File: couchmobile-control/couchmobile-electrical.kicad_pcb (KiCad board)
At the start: 2 copper layers, 100 x 100 mm, 50 parts, among them J1 Power_In, J10 Motor1, J11 Motor2, J2 GPIO_NANO_1, J5 ESTOP_IRQ_EN, J6 BNO_COMM_CTRL, J7 Joystick, J8 Encoder1, J9 Encoder2, Q1 PMOS DGS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

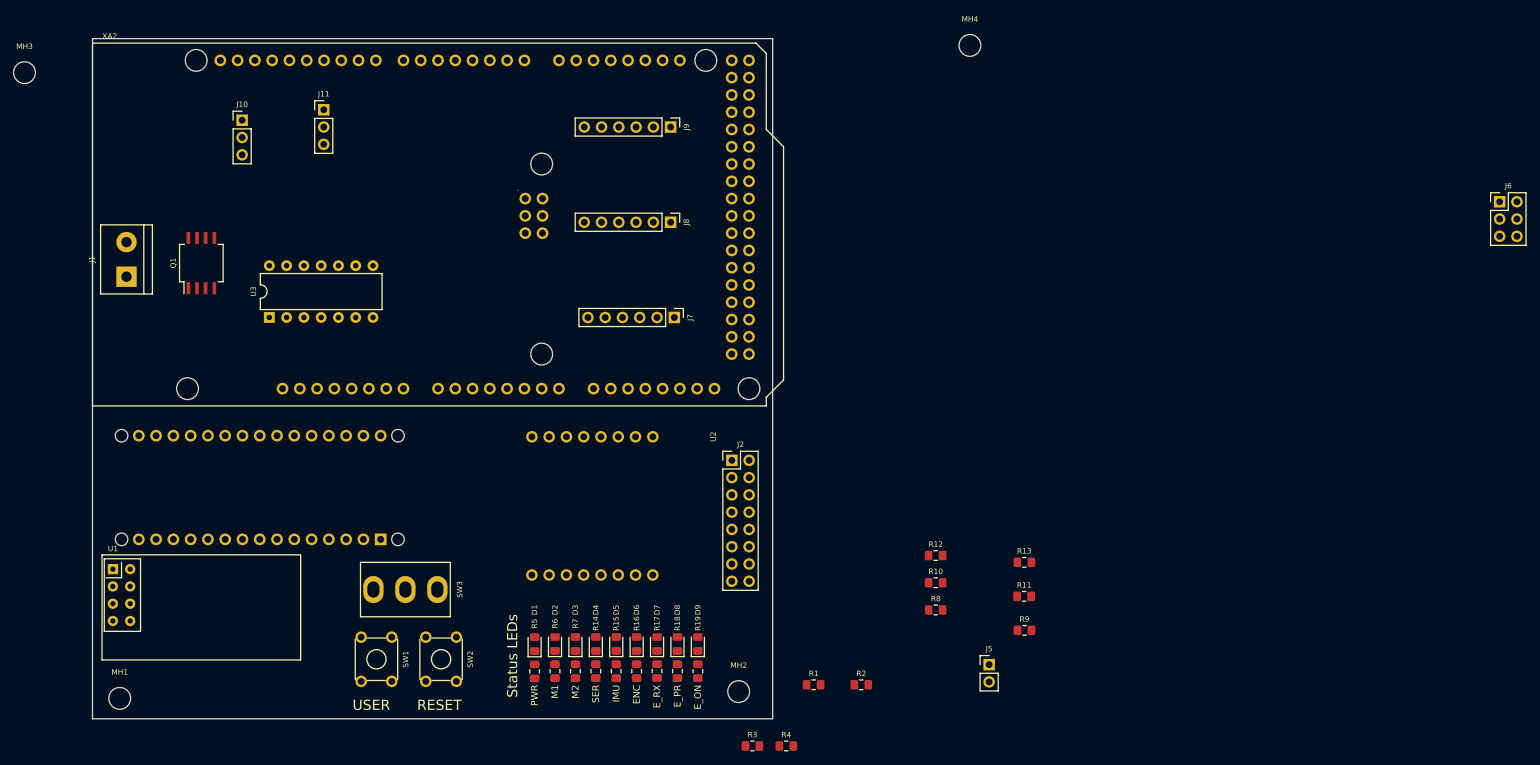
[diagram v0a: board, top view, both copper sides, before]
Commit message: Made and added so8 package for pfet
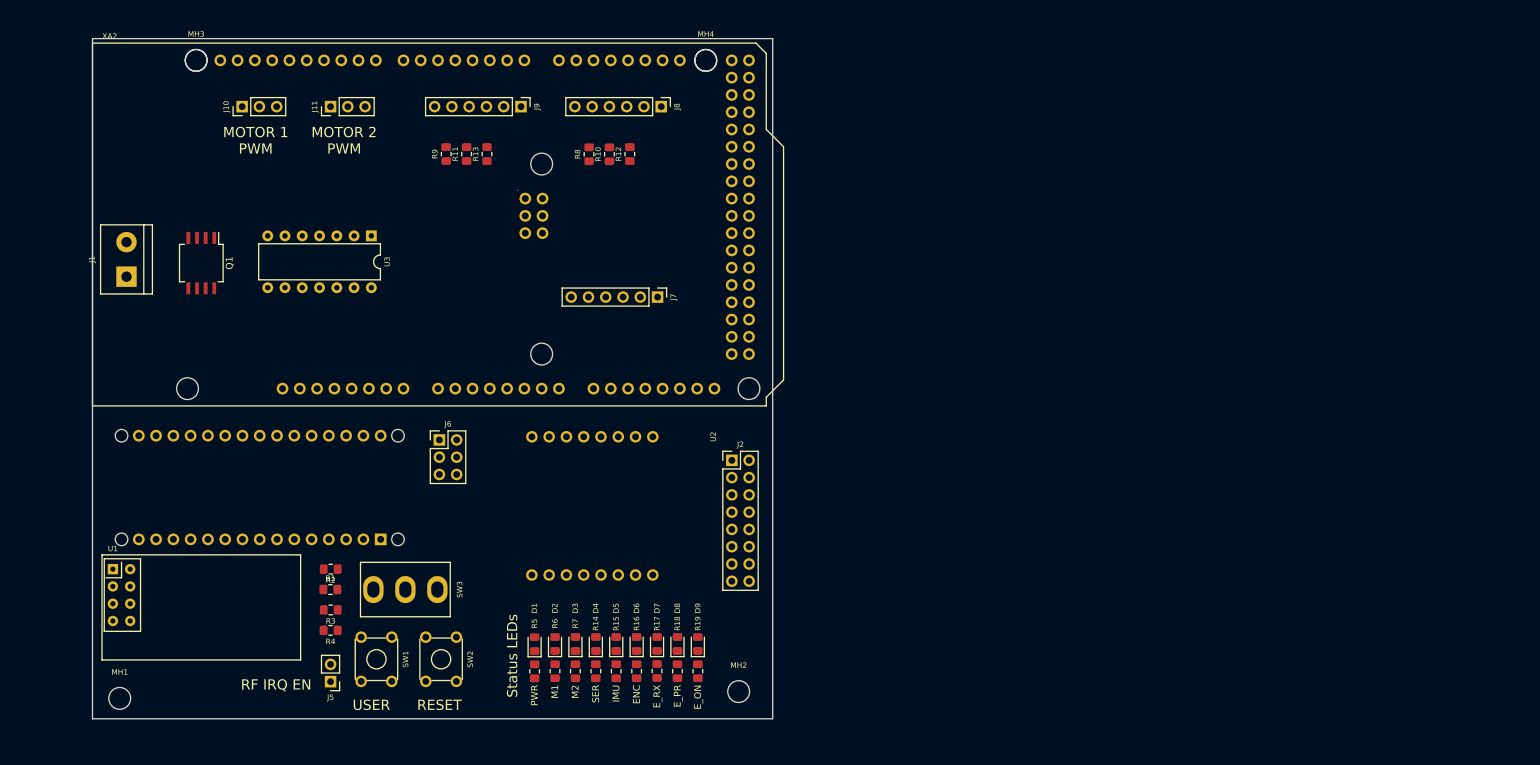
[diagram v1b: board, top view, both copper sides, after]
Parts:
- Q1: footprint Package_SO:SO-8_5.3x6.2mm_P1.27mm -> couch-packages:SO-8_DGS
- moved J6 159.8 mm to (71.0, 79.0)
- moved R9 110.1 mm to (72.0, 37.0), turned to 90 degrees
- moved R11 104.6 mm to (75.0, 37.0), turned to 90 degrees
- moved R13 99.2 mm to (78.0, 37.0), turned to 90 degrees
- moved J5 96.9 mm to (55.0, 114.5), turned to 180 degrees
- moved R8 84.2 mm to (93.0, 37.0), turned to 90 degrees
- moved R2 79.8 mm to (55.0, 98.0), turned to 180 degrees
- moved R10 79.2 mm to (96.0, 37.0), turned to 90 degrees
- moved R12 74.2 mm to (99.0, 37.0), turned to 90 degrees
- moved R1 72.4 mm to (55.0, 101.0)
- moved R4 69.1 mm to (55.0, 107.0), turned to 180 degrees
- moved R3 65.1 mm to (55.0, 104.0), turned to 180 degrees
- moved MH4 38.9 mm to (110.2, 23.2)
- moved MH3 25.3 mm to (35.2, 23.2)
- moved J9 22.2 mm to (83.0, 30.0)
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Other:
- board text added: "MOTOR 1 PWM"
- board text added: "MOTOR 2 PWM"
- board text added: "RF IRQ EN"

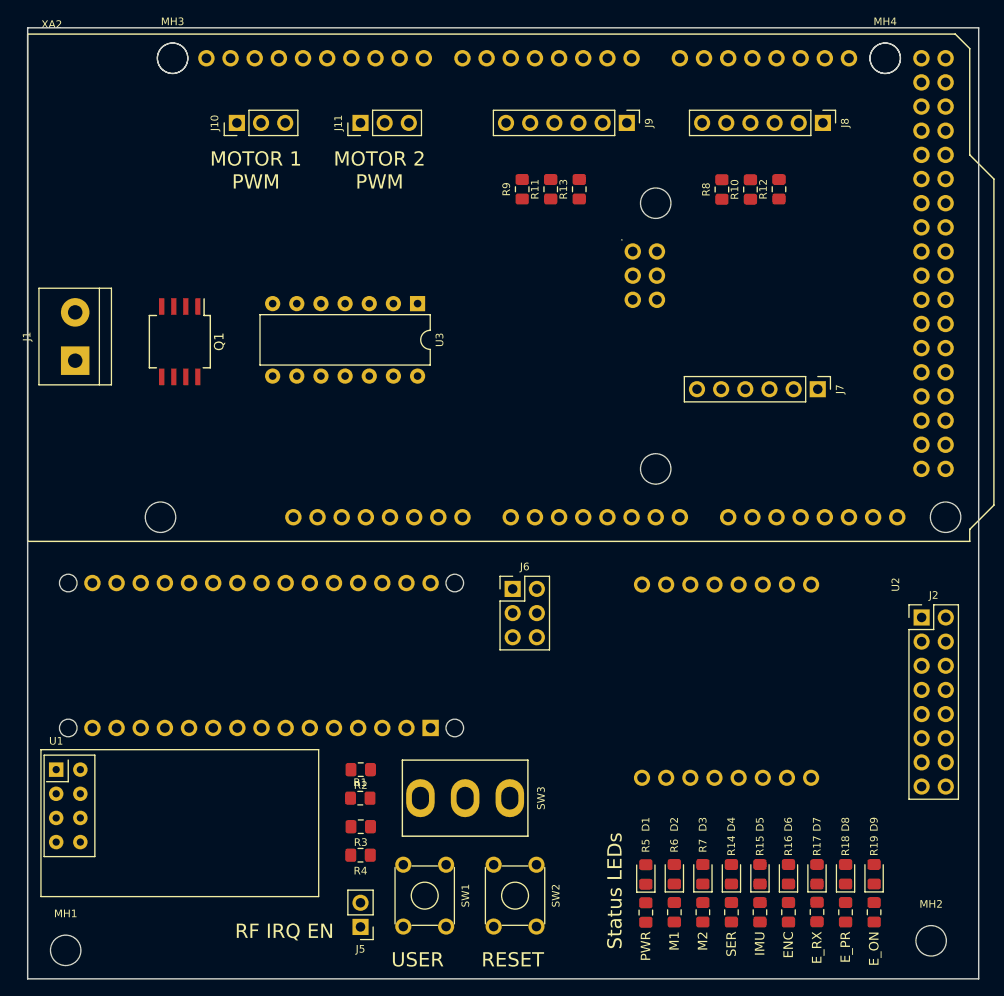
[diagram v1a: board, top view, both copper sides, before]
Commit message: Changed solder to mask clearance to 0.05mm. Wired up half the gpio for nano
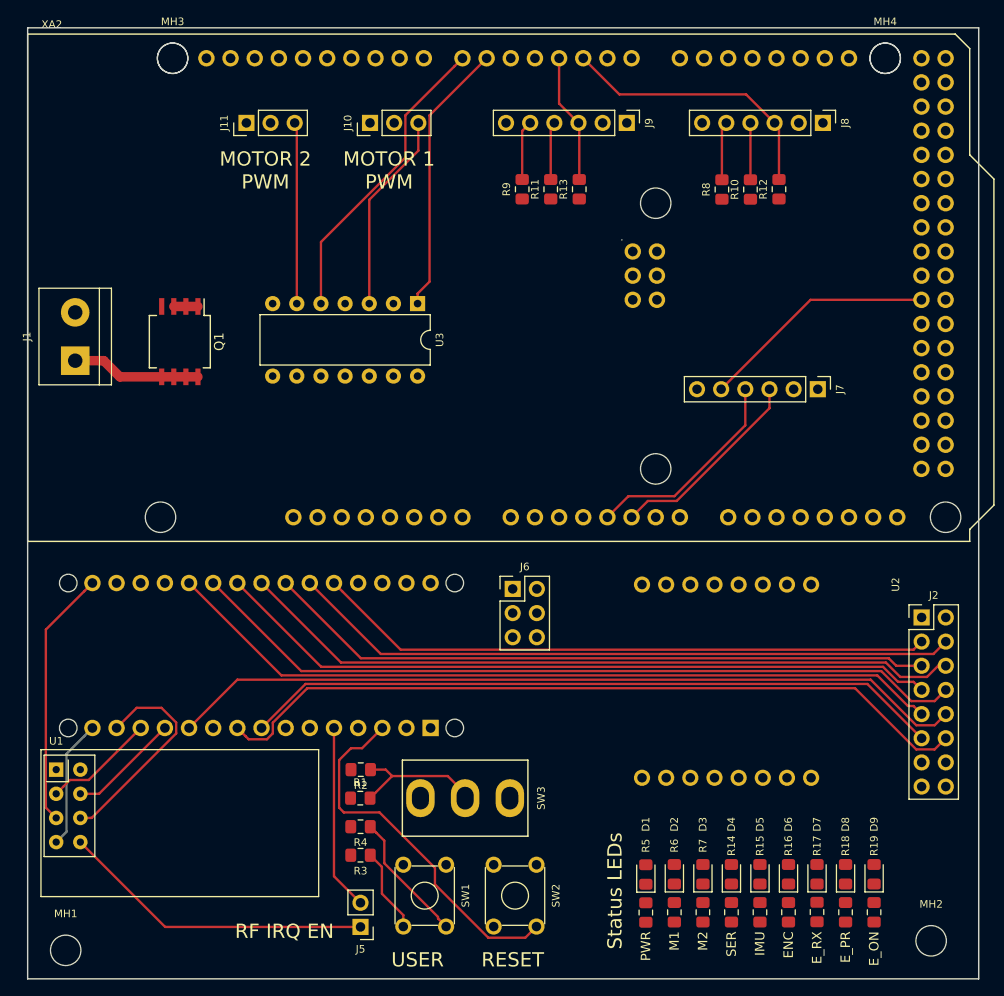
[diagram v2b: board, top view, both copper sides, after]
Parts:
- moved J10 14.0 mm to (56.0, 30.0)
- moved J11 12.0 mm to (43.0, 30.0)
- moved R3 3.00 mm to (55.0, 107.0)
- moved R4 3.00 mm to (55.0, 104.0)
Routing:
- net /NANO_D8: track 0.00 -> 84.1 mm
- net /NANO_A1: track 0.00 -> 82.7 mm
- net /NANO_A2: track 0.00 -> 82.7 mm
- net /ESTOP_HS: track 0.00 -> 81.0 mm
- net /NANO_A3: track 0.00 -> 76.6 mm
- net /NANO_A4: track 0.00 -> 76.5 mm
- net /ESTOP_ON: track 0.00 -> 73.7 mm
- net /NANO_A6: track 0.00 -> 70.5 mm
- net /NANO_A5: track 0.00 -> 70.5 mm
- net /NANO_A7: track 0.00 -> 65.0 mm
- net /NANO_RESET: track 0.00 -> 38.9 mm
- net /ESTOP_IRQ: track 0.00 -> 33.2 mm
- net /PWM_M2: track 0.00 -> 32.0 mm
- net /EN1_1: track 0.00 -> 29.1 mm
- net /PWM_M1: track 0.00 -> 28.8 mm
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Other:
- rule pad_to_mask_clearance: 0.2 -> 0.05

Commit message: Wired up a lot of the busses.
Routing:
- net /STATUS_IMU: track 0.00 -> 114.7 mm, vias 0 -> 2
- net /STATUS_SERIAL: track 0.00 -> 111.8 mm, vias 0 -> 2
- net /STATUS_ENC: track 0.00 -> 110.8 mm, vias 0 -> 2
- net /STATUS_M1: track 0.00 -> 110.7 mm, vias 0 -> 3
- net /STATUS_M2: track 0.00 -> 107.0 mm, vias 0 -> 3
- net /ESTOP_EN: track 0.00 -> 85.6 mm, vias 0 -> 2
- net /ESTOP_RX: track 0.00 -> 80.8 mm, vias 0 -> 2
- net /SCL: track 0.00 -> 68.0 mm, vias 0 -> 1
- net /SDA: track 0.00 -> 65.5 mm, vias 0 -> 1
- net /NANO_TX: track 0.00 -> 60.2 mm
- net /NANO_RX: track 0.00 -> 58.9 mm
- net /NANO_SW1: track 13.8 -> 71.3 mm
- net /ESTOP_TRAN: track 0.00 -> 56.4 mm
- net /IMU_WAKE: track 0.00 -> 53.3 mm, vias 0 -> 1
- net /MEGA_RESET: track 0.00 -> 52.1 mm
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
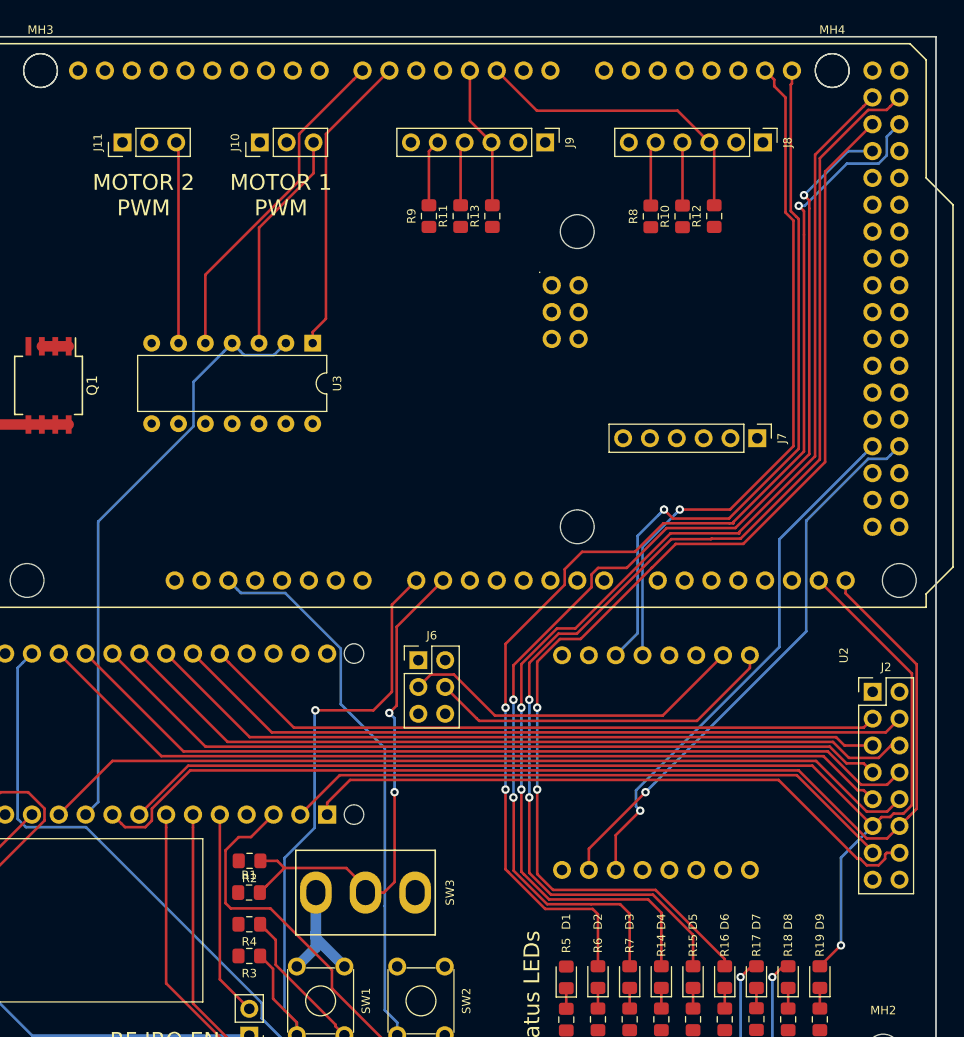
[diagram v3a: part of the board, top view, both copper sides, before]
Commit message: Added 5v to 3.3v line converters.
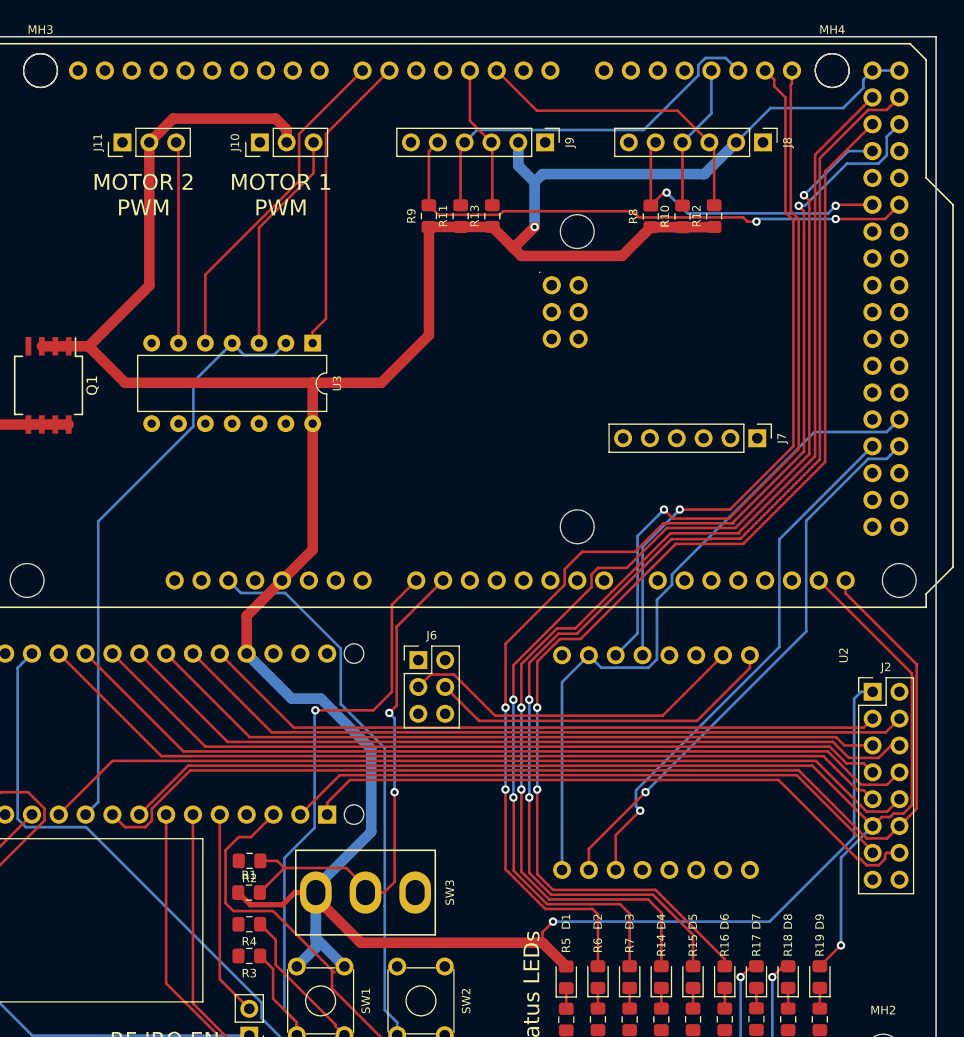
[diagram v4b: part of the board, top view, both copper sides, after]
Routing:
- net +5V: track 14.7 -> 323.7 mm, vias 0 -> 2
- net /IMU_RESET: track 0.00 -> 64.8 mm
- net /EN2_3: track 6.30 -> 52.4 mm, vias 0 -> 2
- net /EN2_2: track 6.11 -> 36.4 mm
- net /EN1_3: track 6.17 -> 28.8 mm, vias 0 -> 2
- net /EN1_2: track 5.98 -> 13.9 mm

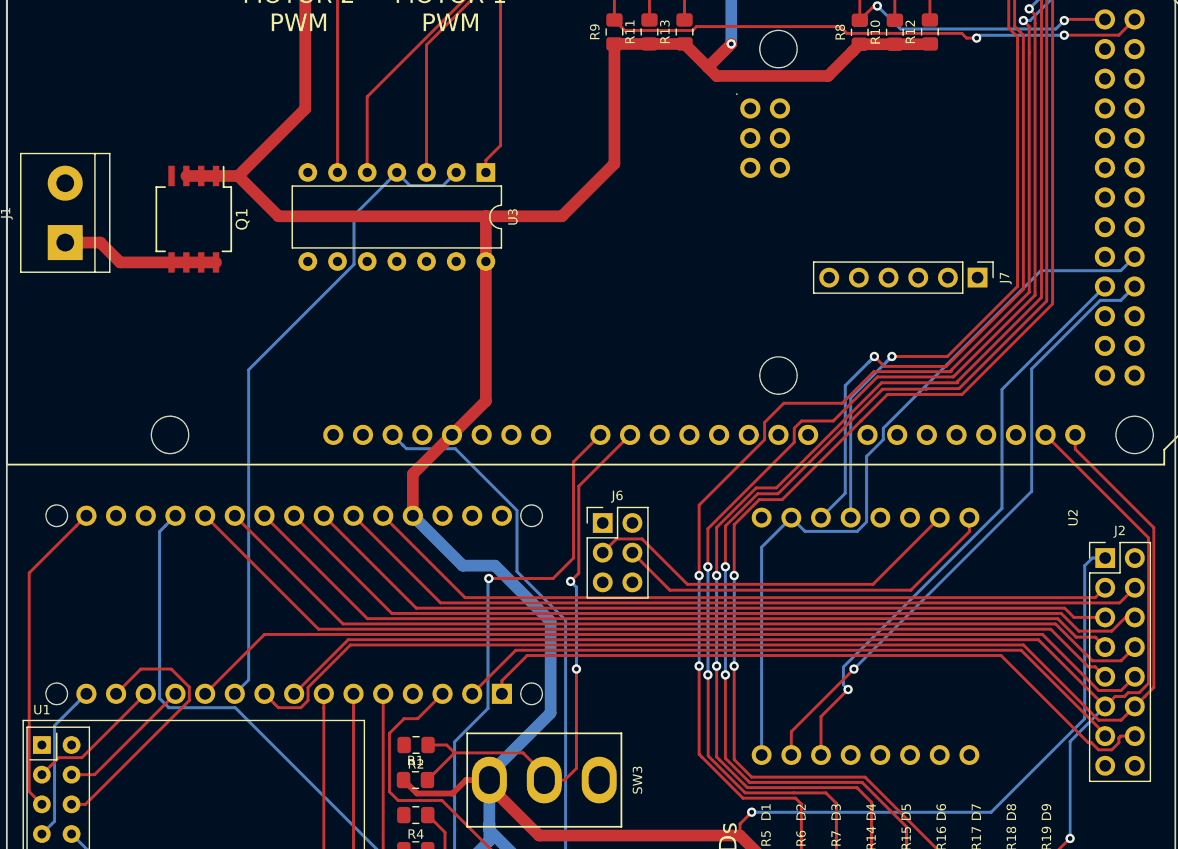
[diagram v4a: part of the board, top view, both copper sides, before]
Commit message: Laid out most lines except ground
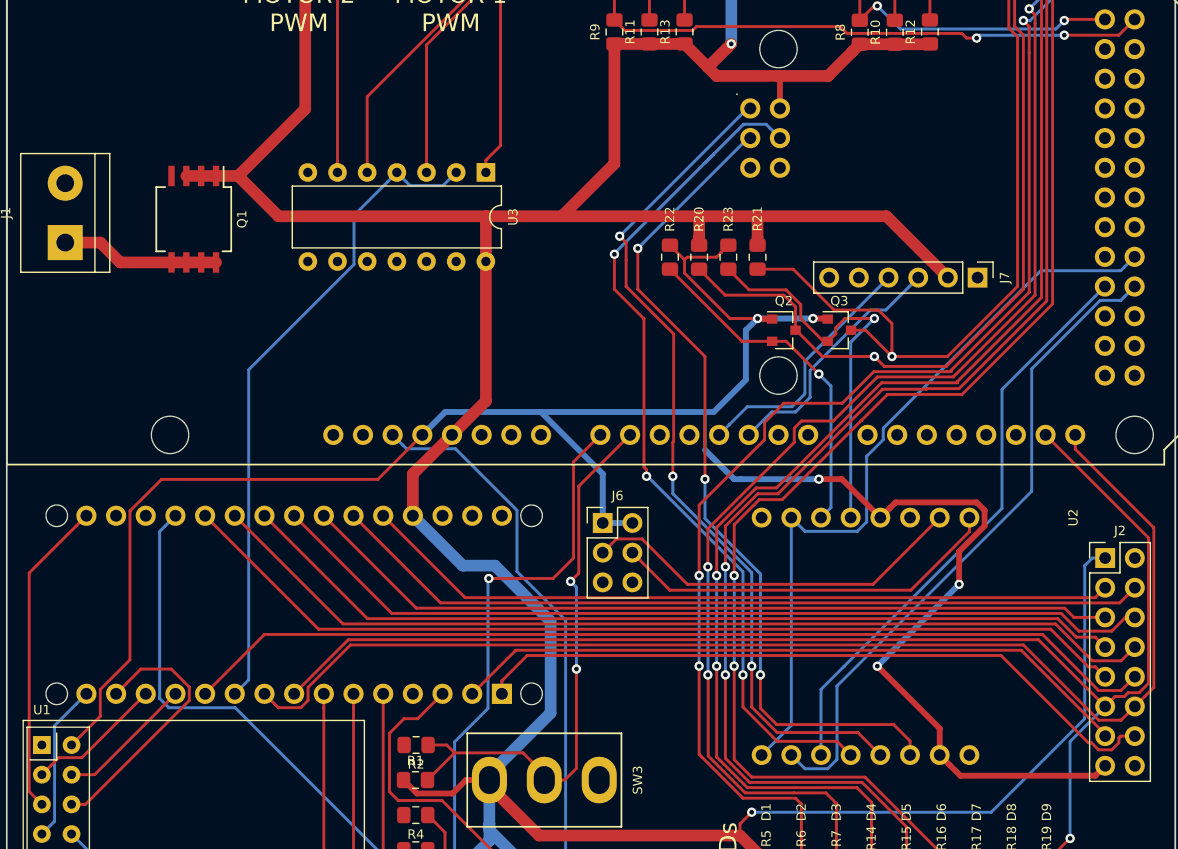
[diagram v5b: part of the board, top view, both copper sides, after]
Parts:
- added Q2: Q_NMOS_GSD, Package_TO_SOT_SMD:SOT-23, F.Cu at (86.5, 62.5)
- added Q3: Q_NMOS_GSD, Package_TO_SOT_SMD:SOT-23, F.Cu at (91.2, 62.5)
- added R20: 10k, Resistor_SMD:R_0805_2012Metric_Pad1.15x1.40mm_HandSolder, F.Cu at (79.2, 56.2)
- added R21: 10k, Resistor_SMD:R_0805_2012Metric_Pad1.15x1.40mm_HandSolder, F.Cu at (84.2, 56.2)
- added R22: 10k, Resistor_SMD:R_0805_2012Metric_Pad1.15x1.40mm_HandSolder, F.Cu at (76.8, 56.2)
- added R23: 10k, Resistor_SMD:R_0805_2012Metric_Pad1.15x1.40mm_HandSolder, F.Cu at (81.8, 56.2)
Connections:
- U2 pad 4: /SDA -> /SDA_3V3
- U2 pad 5: /SCL -> /SCL_3V3
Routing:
- net +3V3: track 0.00 -> 194.3 mm, vias 0 -> 5
- net /MOSI: track 0.00 -> 74.6 mm, vias 0 -> 3
- net /MISO: track 0.00 -> 73.5 mm, vias 0 -> 3
- net /SCK: track 0.00 -> 72.4 mm, vias 0 -> 3
- net +5V: track 323.7 -> 366.7 mm
- net /SDA_3V3: track 0.00 -> 34.8 mm, vias 0 -> 1
- net /SCL_3V3: track 0.00 -> 29.5 mm, vias 0 -> 1
- net /JOYSTICK_Y: track 0.00 -> 21.7 mm
- net /JOYSTICK_X: track 0.00 -> 21.4 mm
- net /SDA: track 65.5 -> 70.6 mm
- net /IMU_WAKE: track 53.3 -> 56.8 mm, vias 1 -> 0
- net /SCL: track 68.0 -> 71.3 mm
- net /IMU_CS: track 50.5 -> 50.3 mm, vias 1 -> 0

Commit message: Poured ground and did DRC. Fixed all markers.
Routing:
- net /JOYSTICK_SW: track 0.00 -> 31.7 mm
- net GND: track 0.00 -> 18.2 mm, vias 0 -> 110
- net /NANO_SW1: track 71.3 -> 80.3 mm
- net /ESTOP_IRQ: track 33.2 -> 36.0 mm
- net /MEGA_SW2: track 48.8 -> 50.1 mm
- added copper zone on B.Cu, net GND
- added copper zone on F.Cu, net GND
